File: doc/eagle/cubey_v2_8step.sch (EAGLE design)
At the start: 33 parts, among them K1 PIN20X2

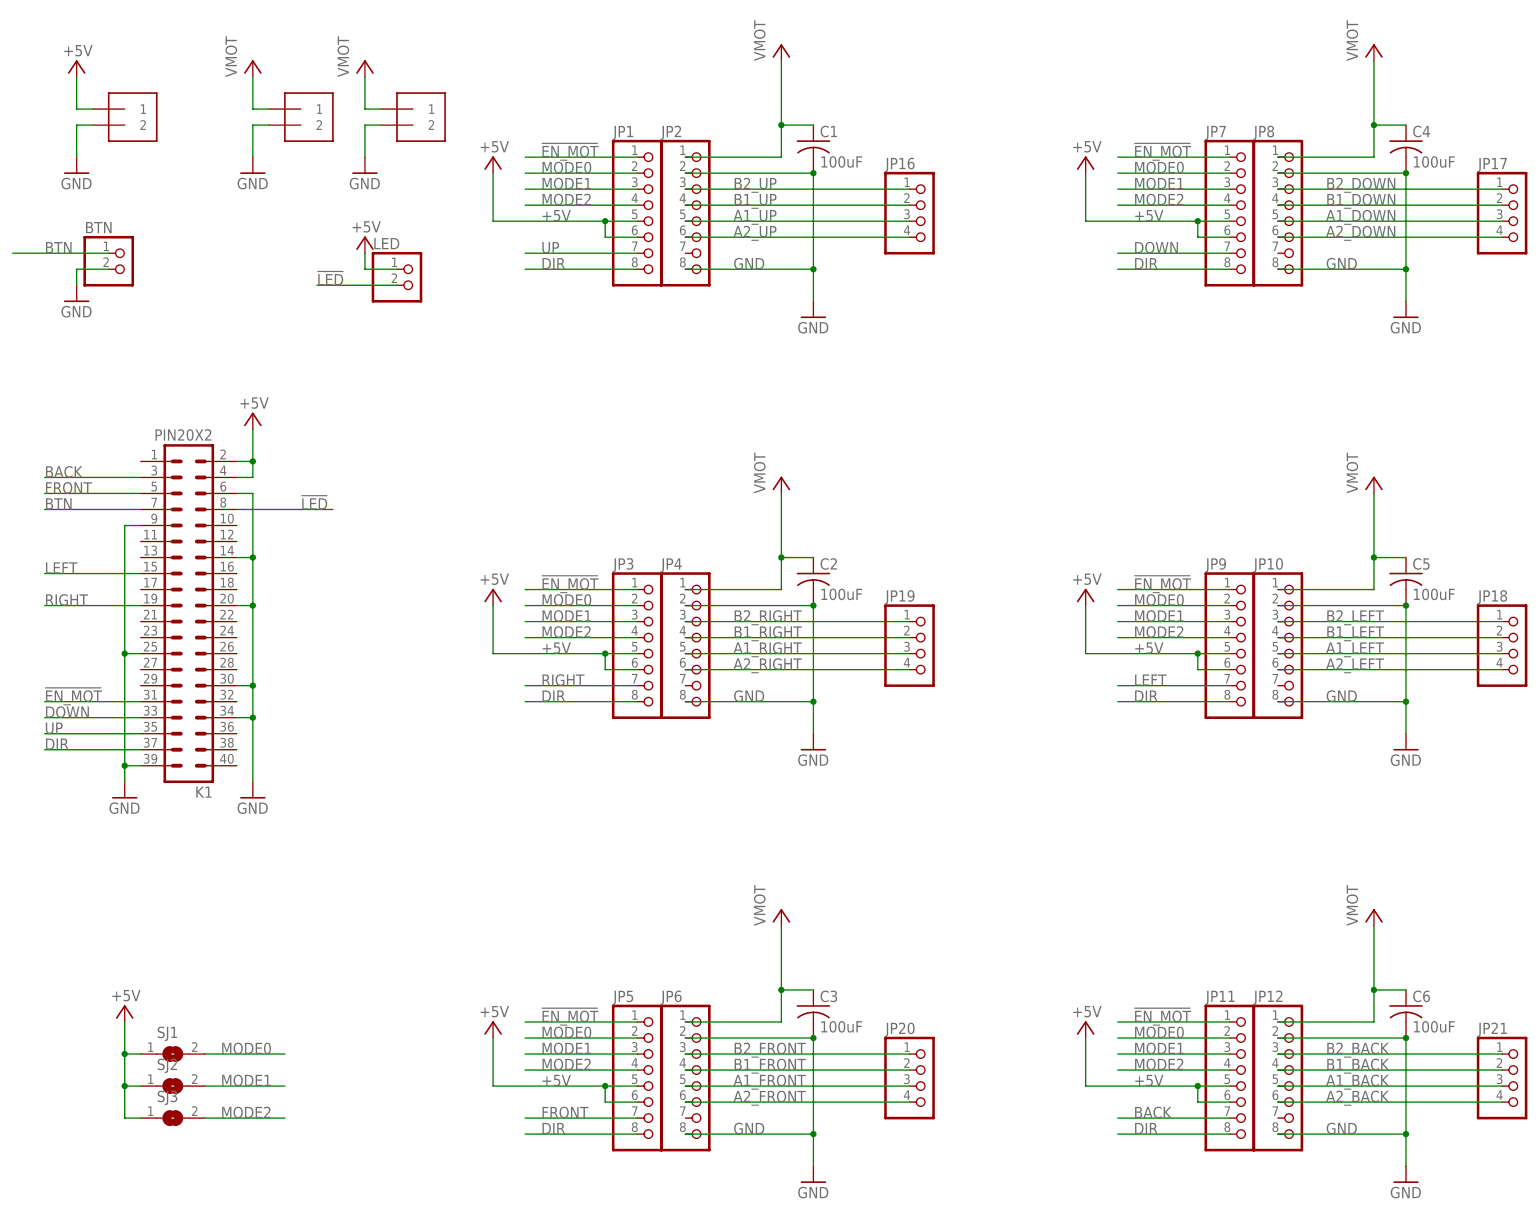
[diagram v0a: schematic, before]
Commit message: Added links to Fusion 360 CAD files, updated Cubey PCB EAGLE files.
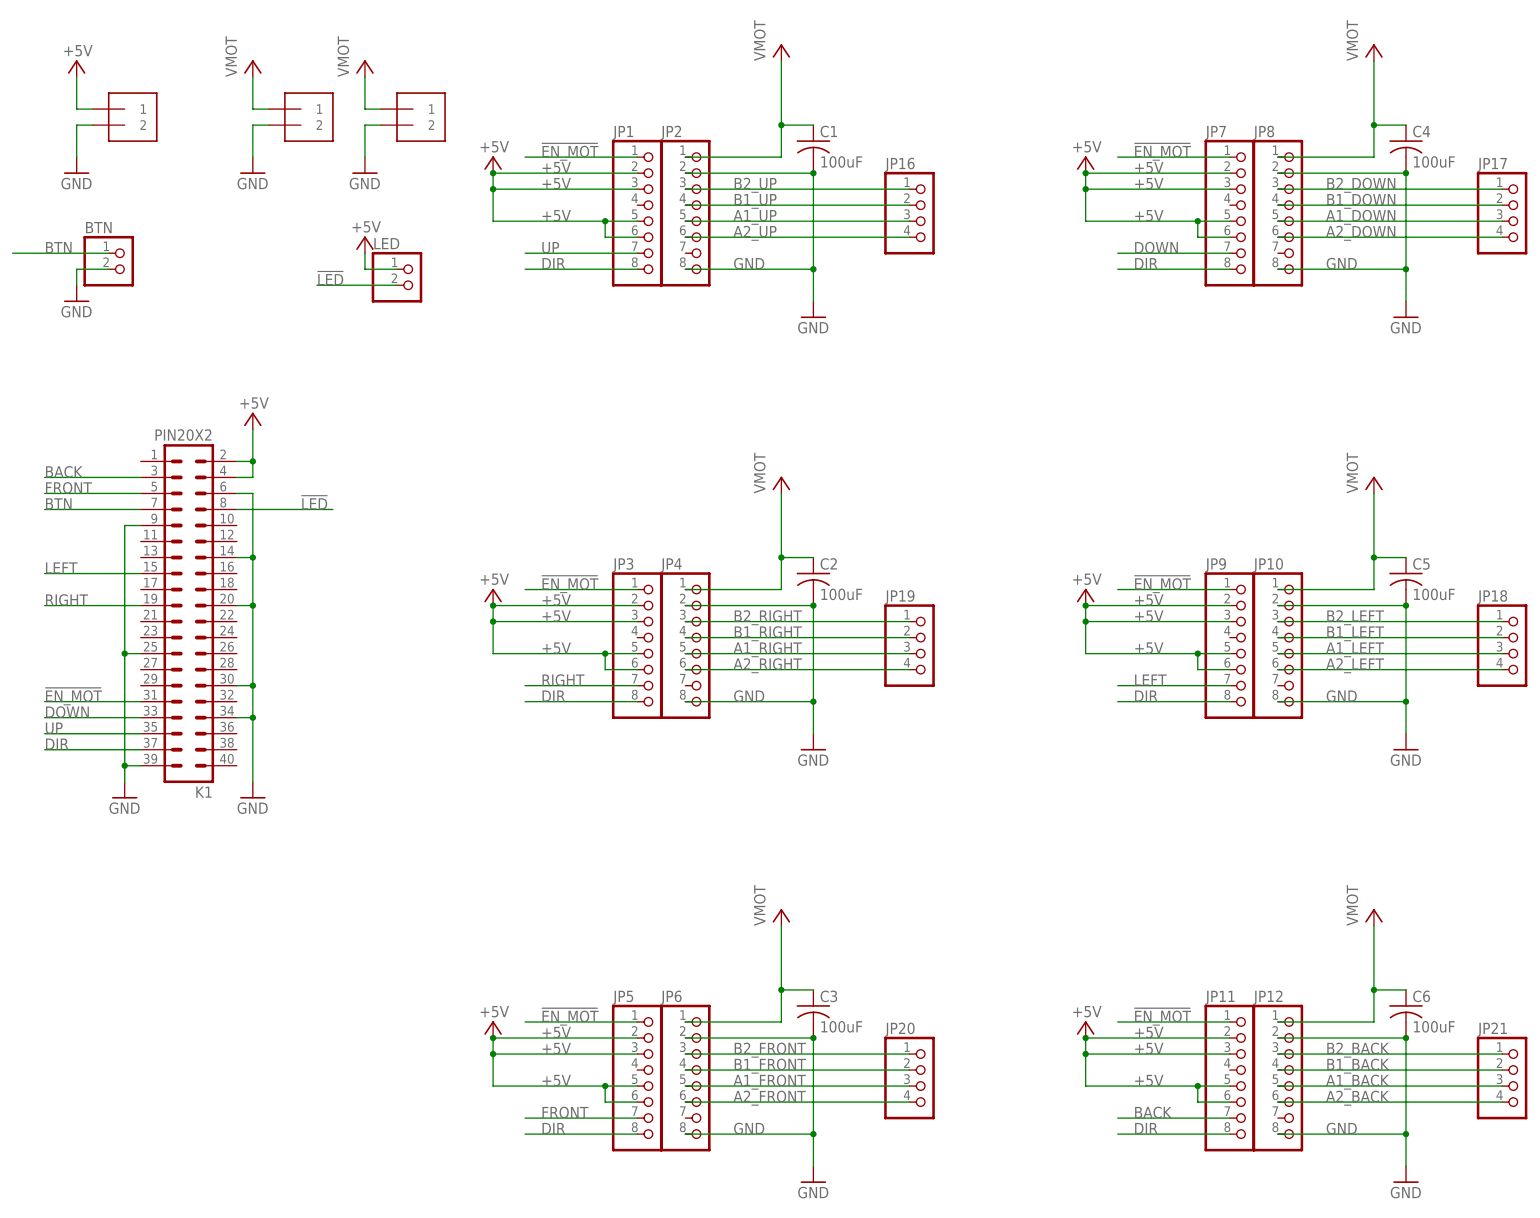
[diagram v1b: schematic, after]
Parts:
- removed SJ1, SJ2, SJ3: (no value), jumper:SJ
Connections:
- removed net MODE0: JP1.2, JP11.2, JP3.2, JP5.2, JP7.2, JP9.2, SJ1.2
- removed net MODE1: JP1.3, JP11.3, JP3.3, JP5.3, JP7.3, JP9.3, SJ2.2
- removed net MODE2: JP1.4, JP11.4, JP3.4, JP5.4, JP7.4, JP9.4, SJ3.2
- net +5V: now also JP1.2, JP1.3, JP11.2, JP11.3, JP3.2, JP3.3, JP5.2, JP5.3, JP7.2, JP7.3, JP9.2, JP9.3; no longer SJ1.1, SJ2.1, SJ3.1
